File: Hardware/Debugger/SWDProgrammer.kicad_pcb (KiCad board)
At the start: 4 copper layers, 24.3 x 31 mm, 42 parts, among them J1 USB_C_Receptacle_USB2.0, J2 USB_C_Receptacle_USB2.0, U1 AP2112K-3.3, U2 STM32F103C8Tx, Y1 32.768KHZ, Y2 8Mhz

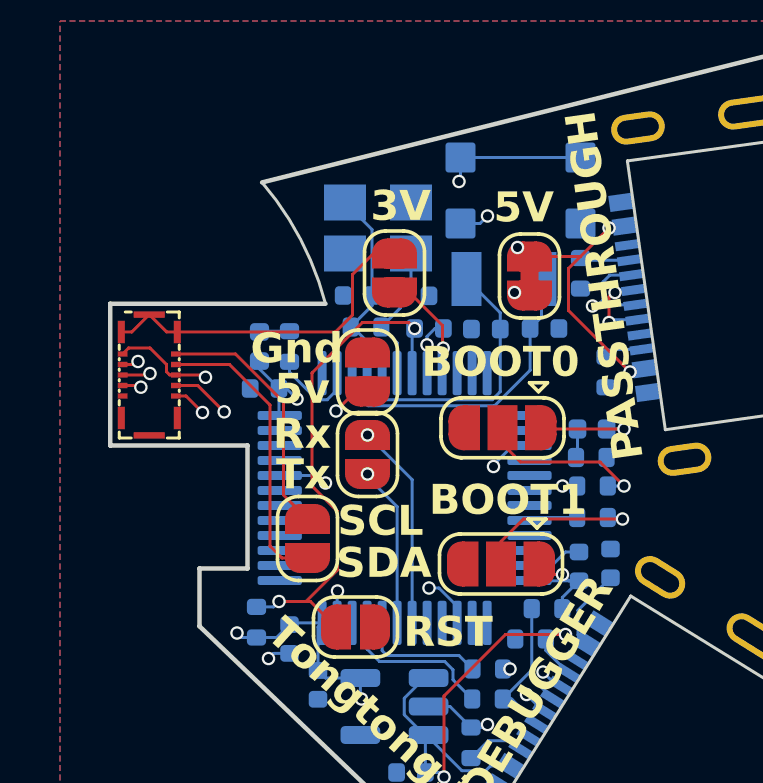
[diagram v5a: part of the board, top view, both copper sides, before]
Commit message: added pogo charging pins, fixed debug connector
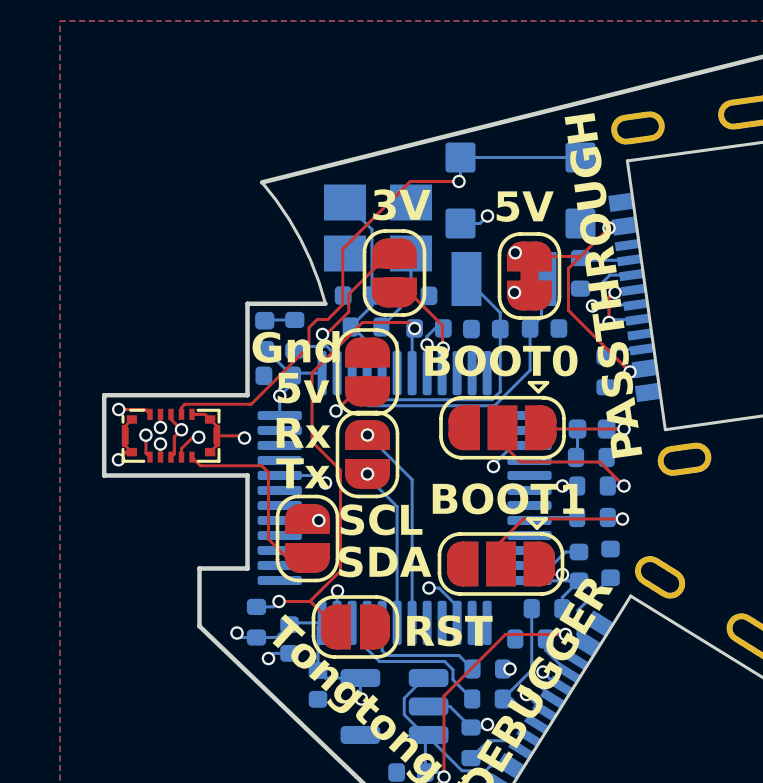
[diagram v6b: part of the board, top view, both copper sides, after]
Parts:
- U3: footprint Library:BK13C06-10DS -> Library:BK13C06-10DP
- moved U3 2.15 mm to (134.7, 61.8), turned to 0 degrees
- moved C7 0.62 mm to (138.3, 59.8)
- moved D1 0.41 mm to (137.8, 58.5)
- moved R3 0.41 mm to (138.8, 58.5)
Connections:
- U2 pad 1: 3VB -> 3.3V
- U3 pad 1: 5V(2) -> D-
- U3 pad 10: D- -> SDA
- U3 pad 2: swc -> D+
- U3 pad 3: swd -> 5V(2)
- U3 pad 6: SCL -> swd
- U3 pad 7: SDA -> swc
- U3 pad 9: D+ -> SCL
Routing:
- net D-: track 20.3 -> 24.9 mm
- net VDD_nRF: track 11.5 -> 15.3 mm, vias 0 -> 2
- net SDA: track 9.81 -> 6.54 mm
- net GND: track 8.85 -> 11.8 mm, vias 5 -> 6
- net D+: track 20.2 -> 22.7 mm
- net SCL: track 8.48 -> 6.17 mm, vias 0 -> 2
- net swc: track 16.4 -> 14.4 mm
- net 3.3V: track 21.2 -> 23.0 mm
- net swd: track 16.0 -> 14.3 mm
- net Net-(U2-PC13): track 3.01 -> 2.16 mm
- net RESET: track 19.2 -> 18.9 mm, vias 2 -> 1
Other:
- board size 24.3 x 31 mm -> 24.5 x 31 mm

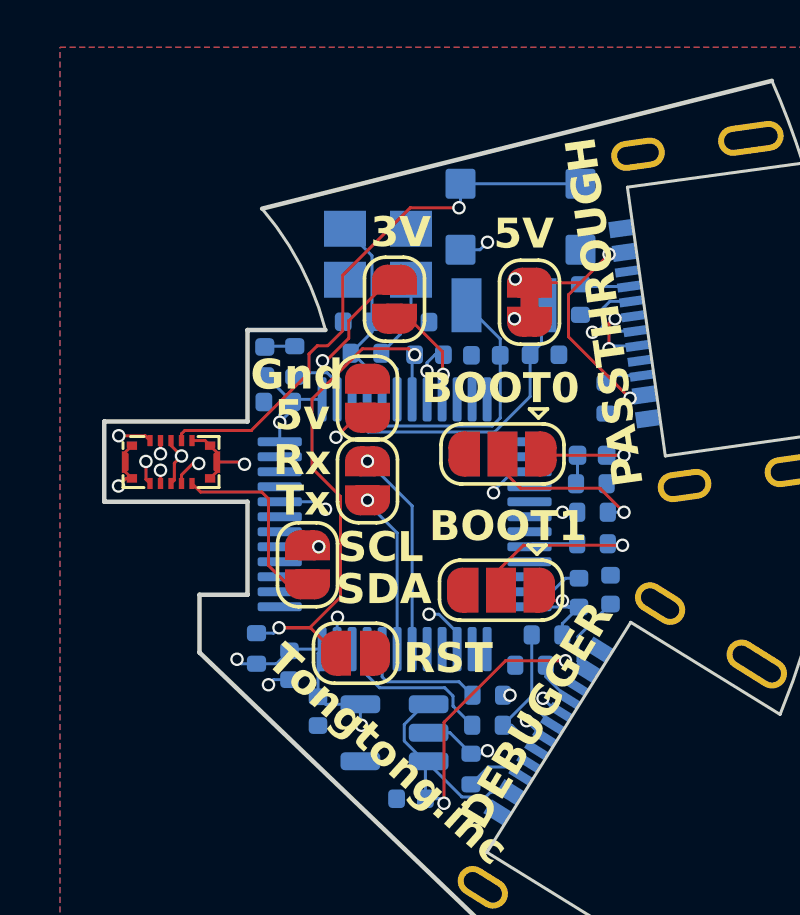
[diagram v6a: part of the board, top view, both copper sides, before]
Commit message: fixed some non existant bugs
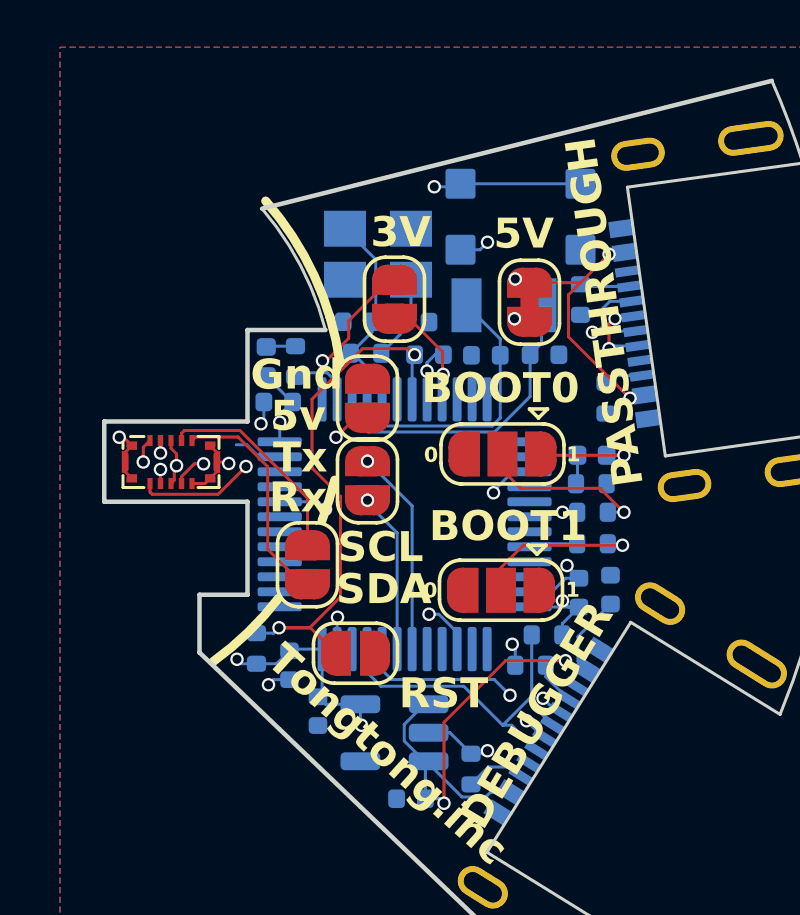
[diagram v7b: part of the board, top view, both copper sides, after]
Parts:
- removed R5, R6: 22Ω, Resistor_SMD:R_0402_1005Metric
- C10, C11: value 9pF -> 22pf
- moved D1 0.05 mm to (137.9, 58.5)
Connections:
- net Net-(U2-PC13) renamed /PC13
- U2 pad 1: 3.3V -> 3VB
- U2 pad 32: Net-(U2-PA11) -> /USBDM
- U2 pad 33: Net-(U2-PA12) -> /USBDP
- U3 pad 1: D- -> swd
- U3 pad 10: SDA -> GND
- U3 pad 2: D+ -> swc
- U3 pad 4: RESET -> SCL
- U3 pad 5: GND -> SDA
- U3 pad 6: swd -> D-
- U3 pad 7: swc -> D+
- U3 pad 9: SCL -> RESET
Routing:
- net /USBDP: track 6.12 -> 12.1 mm
- net Net-(U2-PA12): track 5.26 -> 0.00 mm
- net /USBDM: track 3.89 -> 8.97 mm
- net Net-(U2-PA11): track 4.19 -> 0.00 mm
- net D-: track 24.9 -> 21.6 mm
- net GND: track 11.8 -> 14.9 mm, vias 6 -> 9
- net 3.3V: track 23.0 -> 21.1 mm
- net SDA: track 6.54 -> 7.55 mm
- net VDD_nRF: track 15.3 -> 14.4 mm
- net RESET: track 18.9 -> 19.8 mm, vias 1 -> 2
- net SCL: track 6.17 -> 6.98 mm, vias 2 -> 0
- net D+: track 22.7 -> 22.1 mm
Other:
- board text added: "0"
- board text added: "1"

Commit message: fixed usb datapin issue
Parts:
- S1: value Button -> Button 3x3x1.5
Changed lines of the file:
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@@
         (effects (font (size 1 1) (thickness 0.1)) (justify mirror))
     )
-    (fp_text value "Button" (at -0.45 9 180 unlocked) (layer "B.Fab")
+    (fp_text value "Button 3x3x1.5" (at -0.45 9 180 unlocked) (layer "B.Fab")
         (effects (font (size 1 1) (thickness 0.15)) (justify mirror))
     )
